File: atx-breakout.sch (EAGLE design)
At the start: 103 parts, among them J10 CON_TERMINAL_BLOCK_02-5MM, J3 Molex KK 47053-1000, J4 Molex KK 47053-1000, J5 Molex KK 47053-1000, J6 Molex KK 47053-1000, J8 CON_TERMINAL_BLOCK_02-5MM, J9 CON_TERMINAL_BLOCK_02-5MM, Q1 IRF9530, Q2 IRF9530, Q3 IRF9530, Q4 IRF9530, Q5 IRF9530, Q6 IRF9530, Q7 IRF9530, T1 2N3904, T2 2N3904, T3 2N3904, T4 2N3904, T5 2N3904, T6 2N3904, T7 2N3904, X10 MA02-1JC, X12 XT30-J, X13 MA02-1JC, X15 XT30-J, X16 MA02-1JC, X17 CONN-IDC-10PS, X18 CONN-IDC-10PS, X2 XT30-J, X20 XT30-J, X21 MA02-1JC, X3 MA02-1JC, X4 XT30-J, X5 MA02-1JC, X6 XT30-J, X7 MA02-1JC, X9 XT30-J

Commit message: Everything routed, but need to rething GND
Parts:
- removed X1, X11, X14, X8: (no value), con-amp:USB-787616
- added J1, J11, J2, J7: 61400826021, Wurth_Connectors_WR-USB:61400826021
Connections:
- removed net N$29: C12.1, C6.+, F5.2, LED6.A, X14.1, X15.1, X16.1
- new net SW5V1: C12.1, C6.+, F5.2, J11USBA.VBUS, J11USBB.VBUS, LED6.A, SV1.3, X15.2, X16.1
- net +12V/1: now also Q2.S, R5.2; no longer Q1.S, R2.2
- net +12V/2: now also Q1.S, R2.2; no longer Q2.S, R5.2
- net +5V/1: now also Q6.S, R17.2; no longer Q3.S, R8.2, SV1.3, X18-9.KL
- net +5V/2: now also Q5.S, R14.2; no longer Q4.S, R11.2
- net +5V/3: now also Q4.S, R11.2; no longer Q5.S, R14.2
- net +5V/4: now also Q3.S, R8.2; no longer Q6.S, R17.2
- net +5V_STB: now also X18-9.KL
- net FAN1_SENSE: now also X17-4.KL; no longer X17-1.KL
- net FAN2_CTRL: now also X17-1.KL; no longer X17-4.KL
- net FAN3_SENSE: now also X17-8.KL; no longer X17-5.KL
- net FAN4_CTRL: now also X17-5.KL; no longer X17-8.KL
- net GND: now also J11USBA.GND, J11USBB.GND, J1USBA.GND, J1USBB.GND, J2USBA.GND, J2USBB.GND, J7USBA.GND, J7USBB.GND, X12.1, X15.1, X2.1, X20.1, X4.1, X6.1, X9.1; no longer X1.4, X11.4, X12.2, X14.4, X15.2, X2.2, X20.2, X4.2, X6.2, X8.4, X9.2
- net N$14: now also J1USBA.VBUS, J1USBB.VBUS, X6.2; no longer X1.1, X6.1
- net N$19: now also J2USBA.VBUS, J2USBB.VBUS, X9.2; no longer X8.1, X9.1
- net N$24: now also J7USBA.VBUS, J7USBB.VBUS, X12.2; no longer X11.1, X12.1
- net N$35: now also X20.2; no longer X20.1
- net N$4: now also X2.2; no longer X2.1
- net N$9: now also X4.2; no longer X4.1
- net PWR_GOOD: now also SW2.10, SW2.11, SW2.12, SW2.13, SW2.14, SW2.15, SW2.16, SW2.9, X18-8.KL
- net PWR_ON: no longer SW2.10, SW2.11, SW2.12, SW2.13, SW2.14, SW2.15, SW2.16, SW2.9
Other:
- note added: "TODO: check pin dia, XT30 (currently 1.8 drill) check selected MOSFETs check polarities, XT30 use stacked USB Check cap value for 5 and 3.3v Ground plane/return paths! thickness?"
- note removed: "NB! USE STB OR OTHER 5V? NB - unfiltered!"
- note removed: "todo: check pin dia, XT30 (currently 1.8 drill) check selected MOSFETs Alternative footprint for fuse? check polarities, XT30 use stacked USB Check cap value for 5 and 3.3v 5V or 5V stb på ctrl-header?"
- moved on the sheet: 5V_STB, ATX-1, ATX-10, ATX-11, ATX-12, ATX-13, ATX-14, ATX-15, ATX-16, ATX-17, ATX-18, ATX-19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

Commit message: Separate grounds for every channel
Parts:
- removed SV1: (no value), joakim:MA03-1JC
- added R23, R24, R25, R26, R27, R28, R29: 1k, rcl:R-EU_0207/7
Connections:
- removed net N$32: SV1.2, X17-9.KL
- new net GND1: ATX-19.S, C2.-, J9.2, R24.2, R6.1, T2.E, X4.1, X5.2
- new net GND2: ATX-7.S, C3.-, C9.2, J1USBA.GND, J1USBB.GND, R25.2, R9.1, T3.E, X6.1, X7.2
- new net GND3: ATX-18.S, C10.2, C4.-, J2USBA.GND, J2USBB.GND, R12.1, R26.2, T4.E, X10.2, X9.1
- new net GND4: ATX-17.S, C11.2, C5.-, J7USBA.GND, J7USBB.GND, R15.1, R27.2, T5.E, X12.1, X13.2
- new net GND5: ATX-15.S, C12.2, C6.-, J11USBA.GND, J11USBB.GND, R18.1, R28.2, T6.E, X15.1, X16.2
- new net GNDA: ATX-3.S, C13.2, C8.-, J10.2, R21.1, R29.2, T7.E, X20.1, X21.2
- net +12V/1: no longer C7.+, J3-2.S, J4-2.S, J5-2.S, J6-2.S
- net +12V/2: now also C7.+, J3-2.S, J4-2.S, J5-2.S, J6-2.S
- net +5V_STB: no longer SV1.1
- net GND: now also R23.2; no longer ATX-15.S, ATX-17.S, ATX-18.S, ATX-19.S, ATX-3.S, ATX-5.S, ATX-7.S, C10.2, C11.2, C12.2, C13.2, C2.-, C3.-, C4.-, C5.-, C6.-, C8.-, C9.2, J10.2, J11USBA.GND, J11USBB.GND, J1USBA.GND, J1USBB.GND, J2USBA.GND, J2USBB.GND, J7USBA.GND, J7USBB.GND, J9.2, R12.1, R15.1, R18.1, R21.1, R6.1, R9.1, T2.E, T3.E, T4.E, T5.E, T6.E, T7.E, X10.2, X12.1, X13.2, X15.1, X16.2, X20.1, X21.2, X4.1, X5.2, X6.1, X7.2, X9.1
- net PWR_CTRL_12V1: now also R23.1
- net PWR_CTRL_12V2: now also R24.1
- net PWR_CTRL_3V1: now also R29.1
- net PWR_CTRL_5V1: now also R25.1
- net PWR_CTRL_5V2: now also R26.1
- net PWR_CTRL_5V3: now also R27.1
- net PWR_CTRL_5V4: now also R28.1
- net SW5V1: now also X17-9.KL; no longer SV1.3

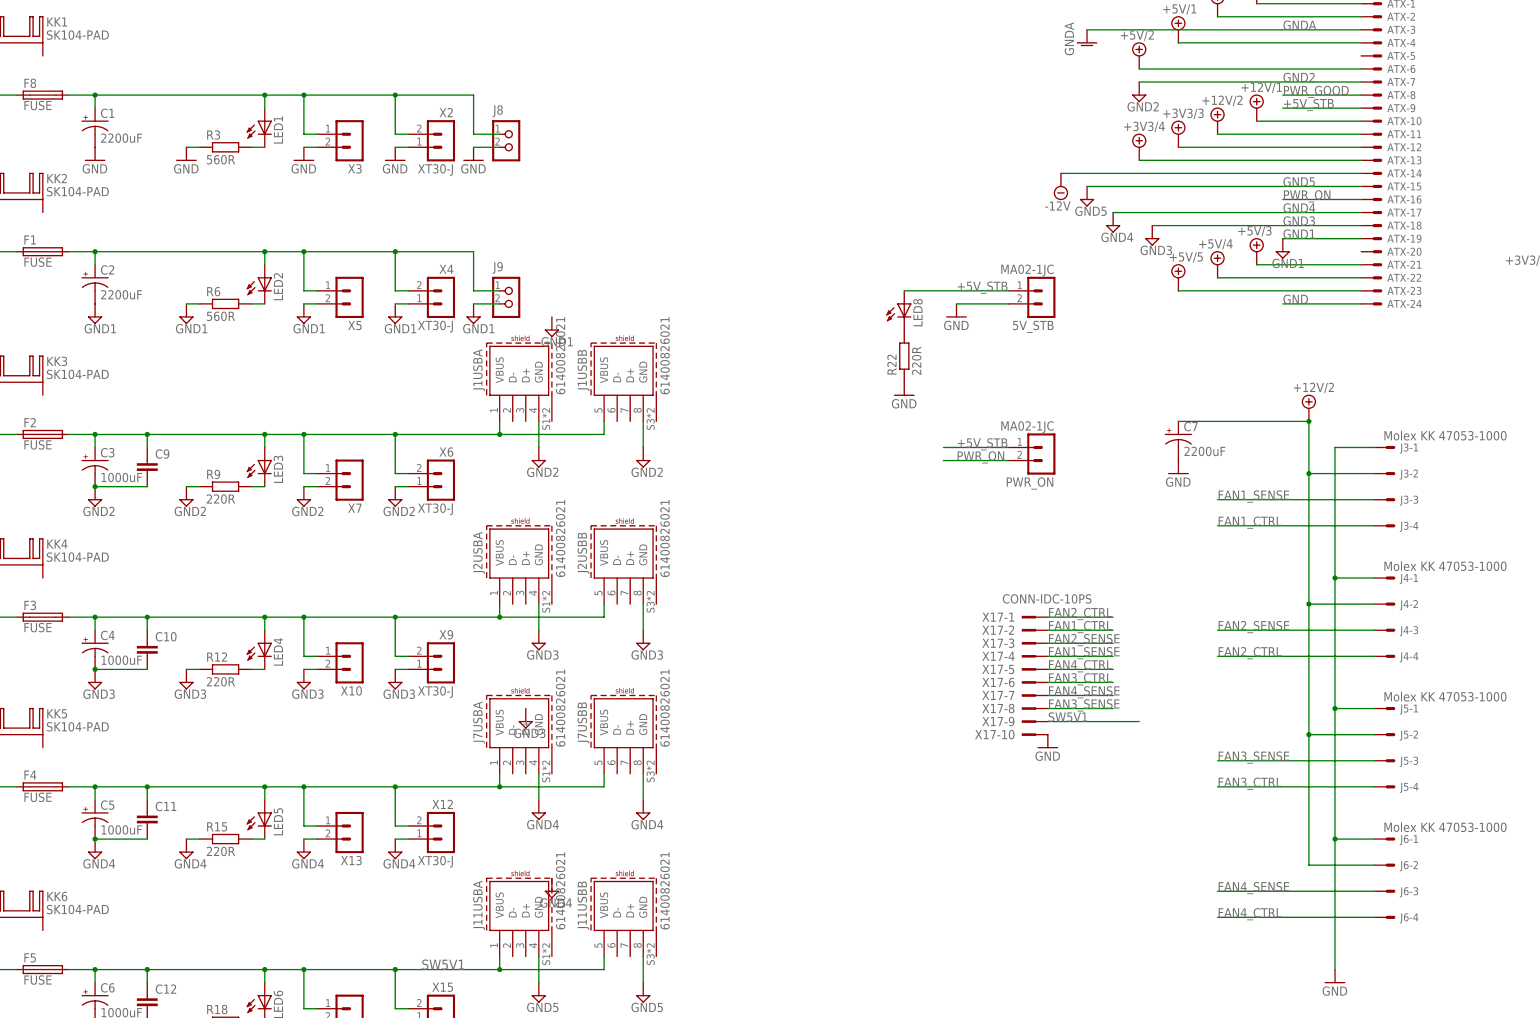
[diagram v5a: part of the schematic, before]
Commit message: More mounting holes, screw terminal for 10Ohm load
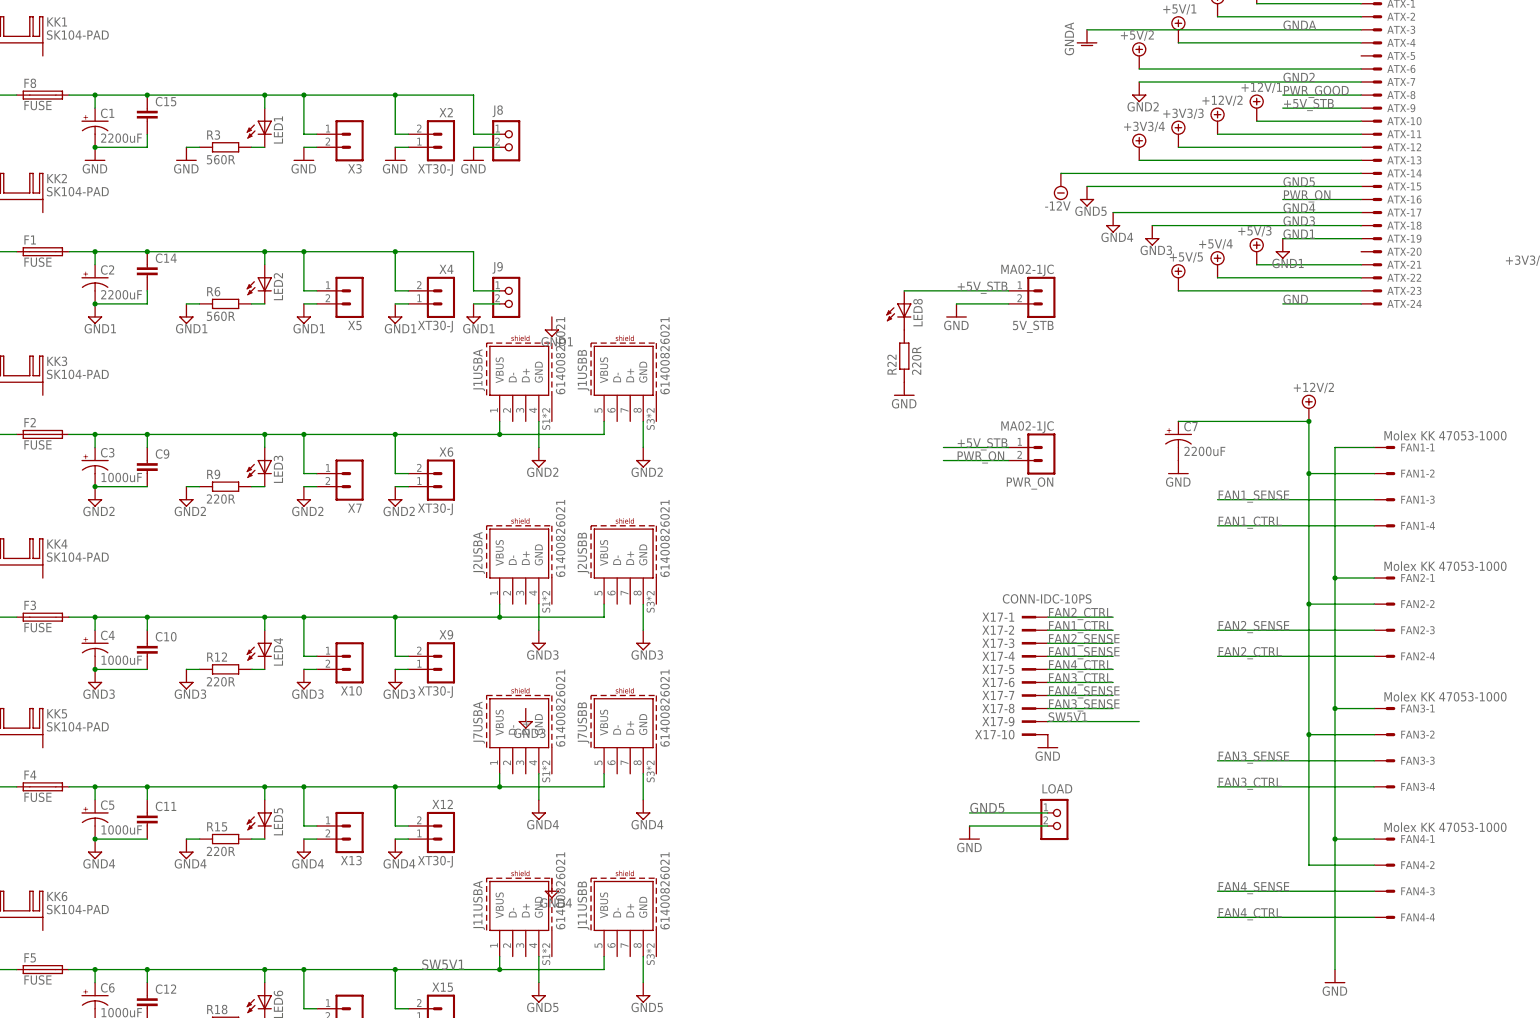
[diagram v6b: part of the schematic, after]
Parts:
- added C14, C15: (no value), rcl:C-EU050-030X075
- added LOAD: CON_TERMINAL_BLOCK_02-5MM, dp_devices.v6:CON_TERMINAL_BLOCK_02-5MM
- renumbered J3 to FAN1, J4 to FAN2, J5 to FAN3, J6 to FAN4
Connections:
- net GND: now also C15.2, LOAD.2
- net GND1: now also C14.2
- net GND5: now also LOAD.1
- net N$4: now also C15.1
- net N$9: now also C14.1

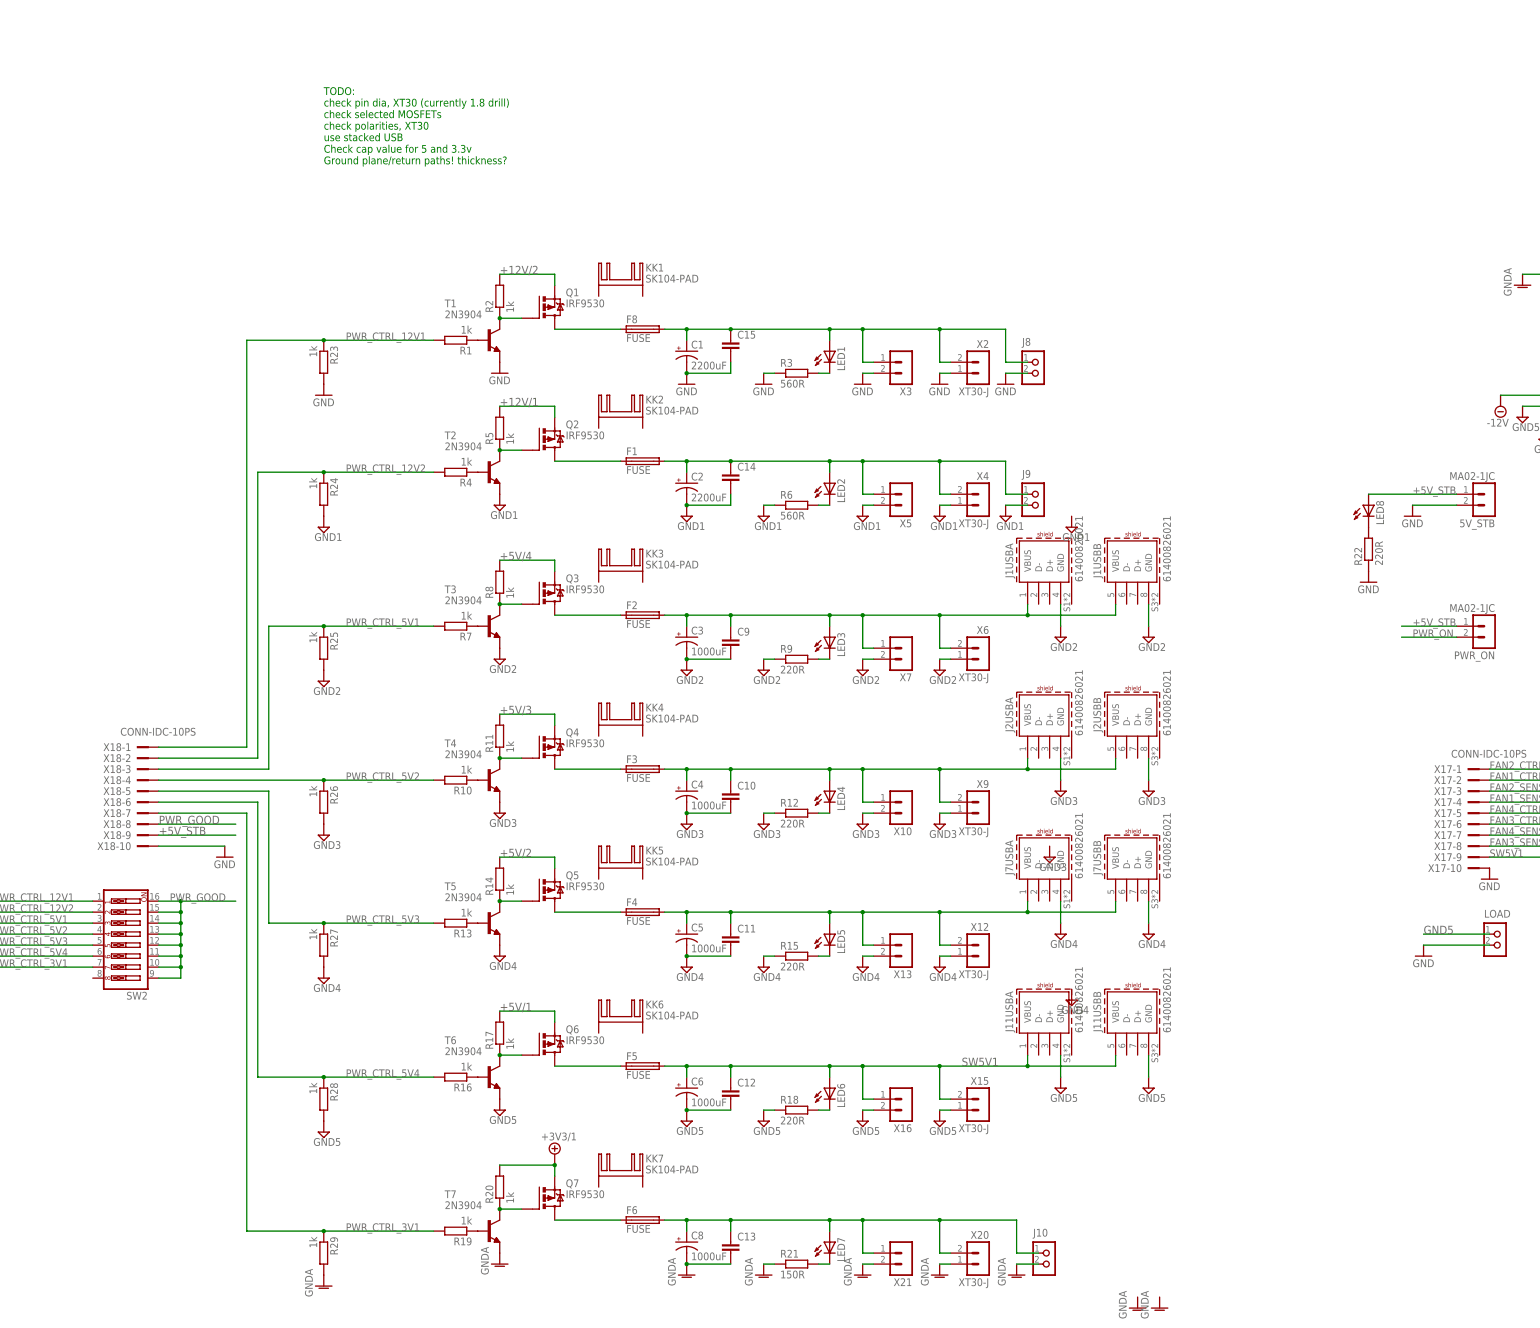
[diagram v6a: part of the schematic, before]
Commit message: Updated XT-30 footprint, updated pulldown resistor value
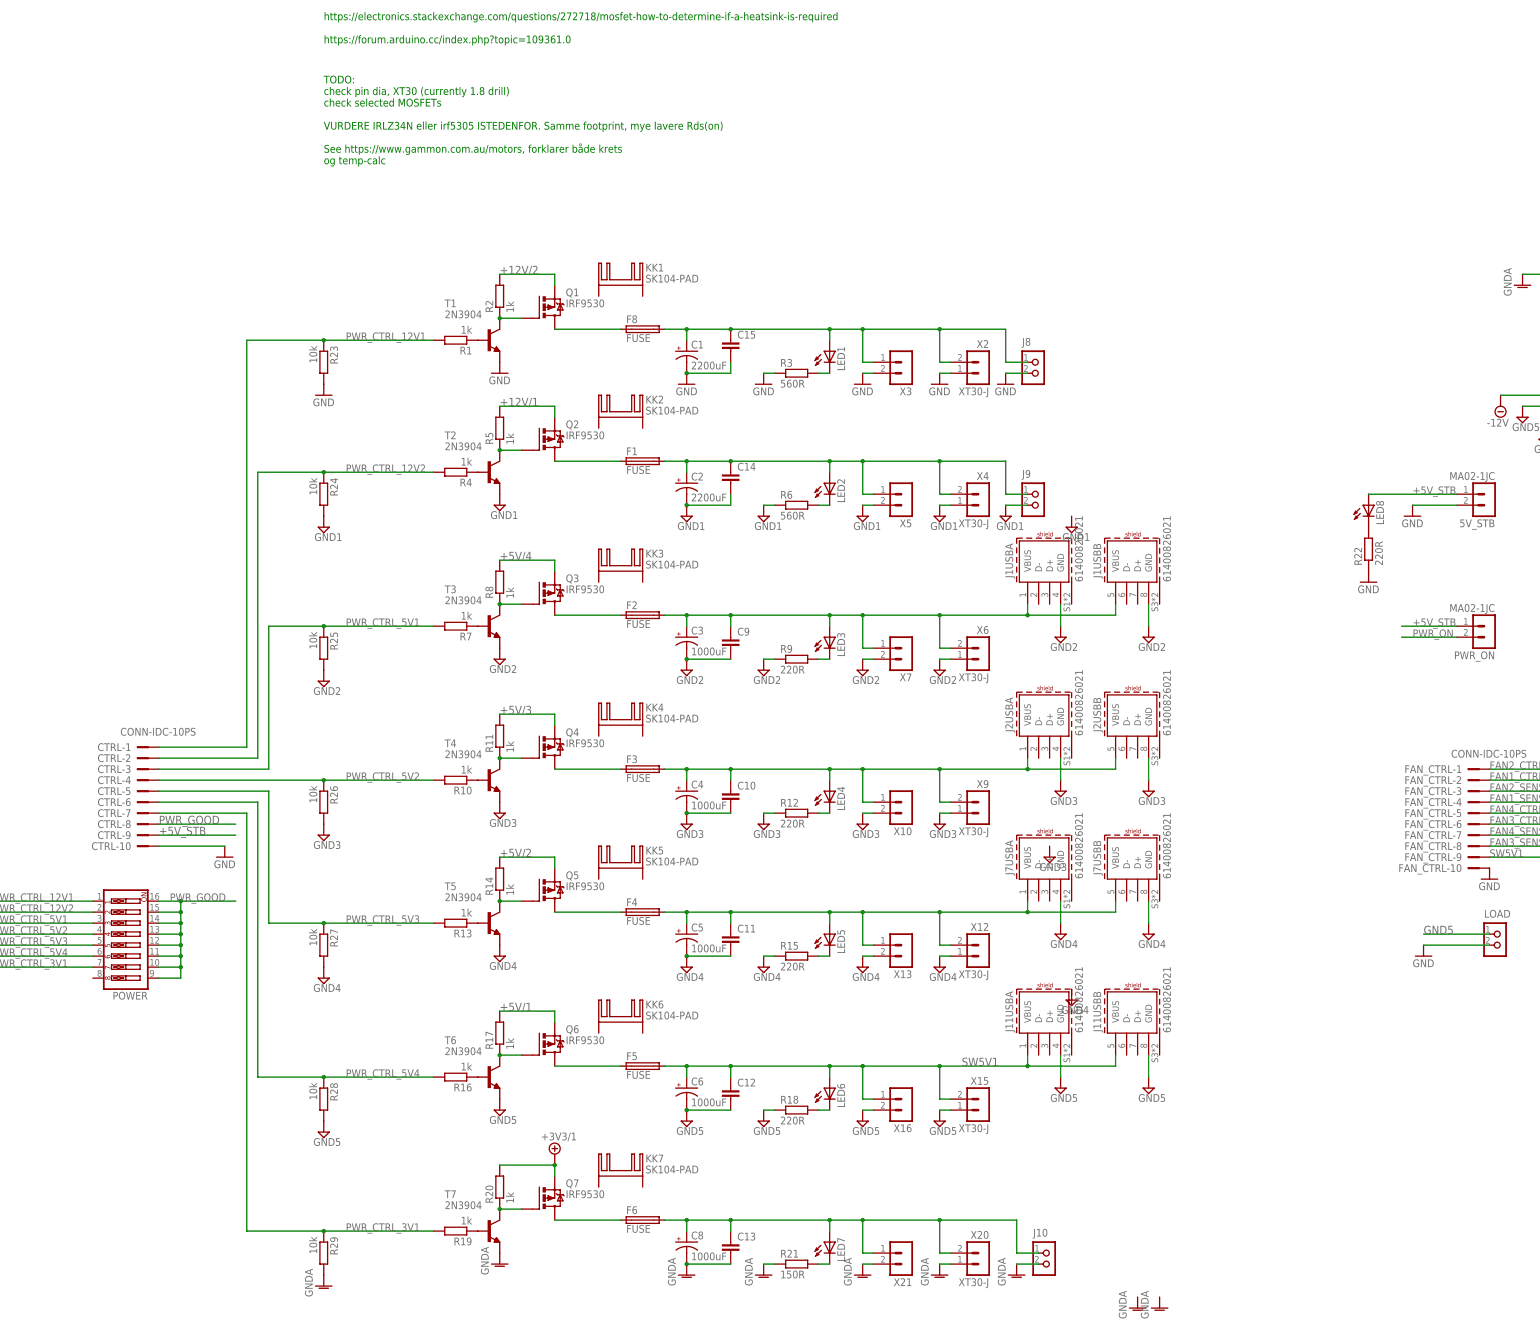
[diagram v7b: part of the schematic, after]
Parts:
- R23, R24, R25, R26, R27, R28, R29: value 1k -> 10k
- renumbered SW2 to POWER, X17 to FAN_CTRL, X18 to CTRL
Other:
- note added: "TODO: check pin dia, XT30 (currently 1.8 drill) check selected MOSFETs VURDERE IRLZ34N eller irf5305 ISTEDENFOR. Samme footprint, mye lavere Rds(on) See https://www.gammon.com.au/motors, forklarer både krets og temp-calc"
- note added: "https://electronics.stackexchange.com/questions/272718/mosfet-how-to-determine-if-a-heatsink-is-required https://forum.arduino.cc/index.php?topic=109361.0"
- note removed: "TODO: check pin dia, XT30 (currently 1.8 drill) check selected MOSFETs check polarities, XT30 use stacked USB Check cap value for 5 and 3.3v Ground plane/return paths! thickness?"
